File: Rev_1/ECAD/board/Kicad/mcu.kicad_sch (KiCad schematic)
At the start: 11 parts, among them Y100 16MHZ

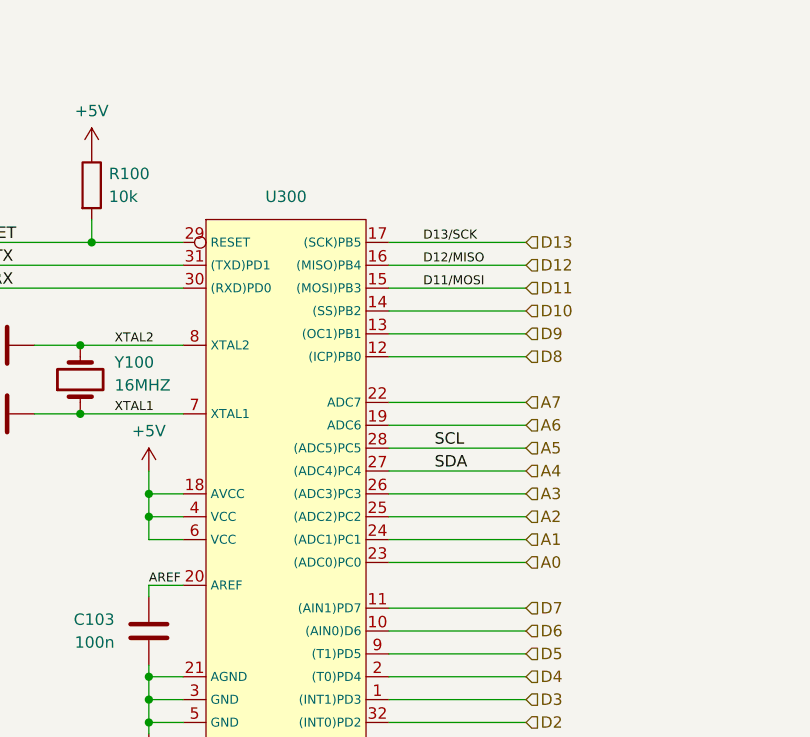
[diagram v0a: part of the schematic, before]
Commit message: Updated Symbol library´and added SD Card Reader to schematic
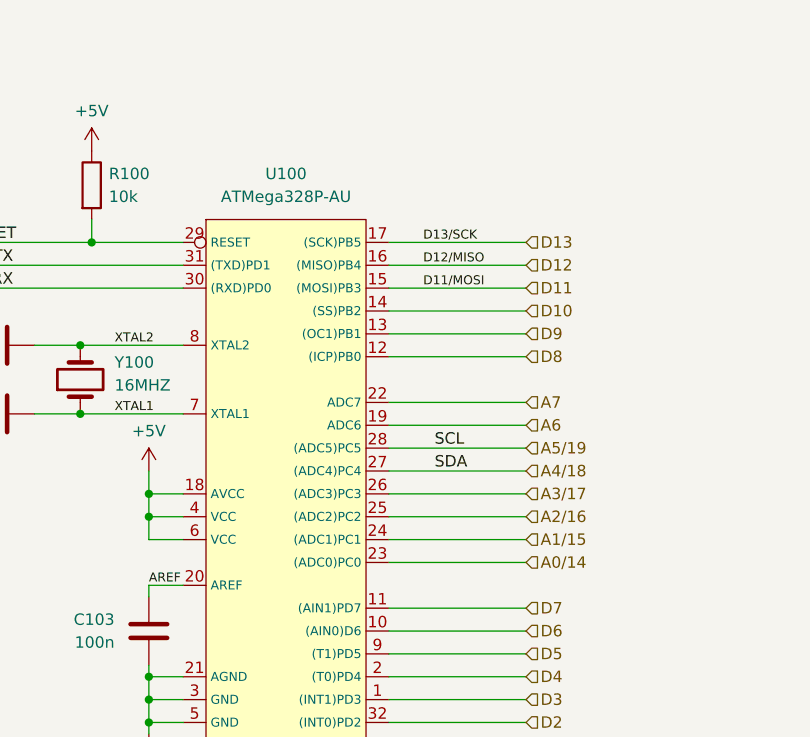
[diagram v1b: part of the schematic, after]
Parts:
- removed U300: ~, symbol EEPROM_PROGRAMER:ATMega328P-AU
- added U100: ATMega328P-AU, symbol EEPROM_PROGRAMMER:ATMega328P-AU
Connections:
- net +5V: now also U100.18 (AVCC), U100.4 (VCC), U100.6 (VCC)
- net A6: now also U100.19 (ADC6)
- net A7: now also U100.22 (ADC7)
- net AREF: now also U100.20 (AREF)
- net D10: now also U100.14 ((SS)PB2)
- net D11: now also U100.15 ((MOSI)PB3)
- net D12: now also U100.16 ((MISO)PB4)
- net D13: now also U100.17 ((SCK)PB5)
- net D2: now also U100.32 ((INT0)PD2)
- net D3: now also U100.1 ((INT1)PD3)
- net D4: now also U100.2 ((T0)PD4)
- net D5: now also U100.9 ((T1)PD5)
- net D6: now also U100.10 ((AIN0)D6)
- net D7: now also U100.11 ((AIN1)PD7)
- net D8: now also U100.12 ((ICP)PB0)
- net D9: now also U100.13 ((OC1)PB1)
- net GND: now also U100.21 (AGND), U100.3 (GND), U100.5 (GND)
- net RESET: now also U100.29 (RESET)
- net RX: now also U100.31 ((TXD)PD1)
- net TX: now also U100.30 ((RXD)PD0)
- net XTAL1: now also U100.7 (XTAL1)
- net XTAL2: now also U100.8 (XTAL2)
- new net A0/14: U100.23 ((ADC0)PC0)
- new net A1/15: U100.24 ((ADC1)PC1)
- new net A2/16: U100.25 ((ADC2)PC2)
- new net A3/17: U100.26 ((ADC3)PC3)
- new net A4/18: U100.27 ((ADC4)PC4)
- new net A5/19: U100.28 ((ADC5)PC5)

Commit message: Changes current limiting resistors for LEDS to 5k1 ohms
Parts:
- U100: footprint (none) -> EEPROM_PROGRAMMER:ATMega328P-AU
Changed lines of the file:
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@@
       (effects (font (size 1.27 1.27)))
     )
-    (property "Footprint" "" (at 143.51 87.63 0)
+    (property "Footprint" "EEPROM_PROGRAMMER:ATMega328P-AU" (at 143.51 87.63 0)
       (effects (font (size 1.27 1.27)) hide)
     )

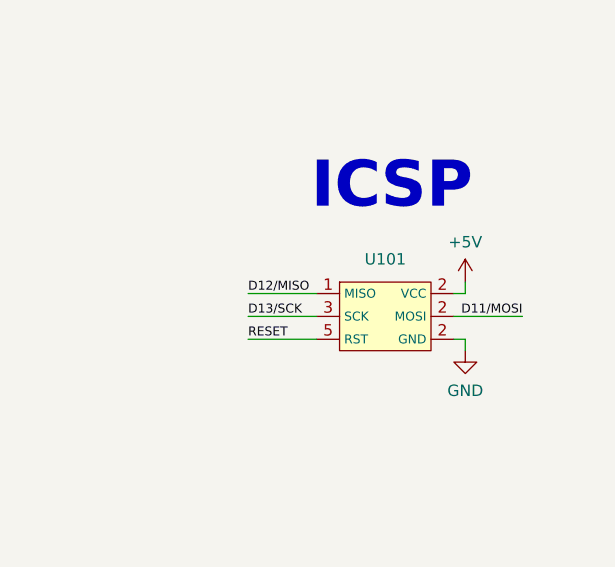
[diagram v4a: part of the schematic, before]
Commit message: Changed from 4-bit registers to shift registers
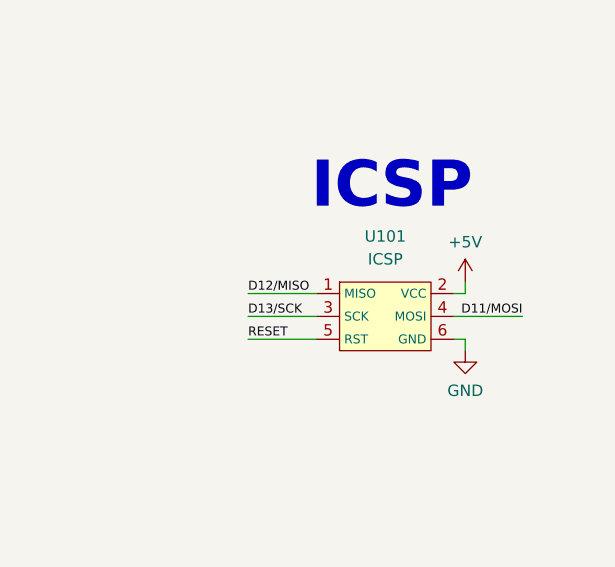
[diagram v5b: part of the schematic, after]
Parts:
- removed U101: ~, symbol EEPROM_PROGRAMER:ICSP
- added U101: ICSP, EEPROM_PROGRAMMER:ICSP, symbol EEPROM_PROGRAMMER:ICSP
- Y100: footprint (none) -> EEPROM_PROGRAMMER:Crystal
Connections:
- net +5V: now also U101.2 (VCC)
- net D11: now also U101.4 (MOSI)
- net D12: now also U101.1 (MISO)
- net D13: now also U101.3 (SCK)
- net GND: now also U101.6 (GND)
- net RESET: now also U101.5 (RST)
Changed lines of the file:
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@@
+    )
+  )
+  (symbol (lib_id "EEPROM_PROGRAMMER:ICSP") (at 234.95 102.87 0) (unit 1)
+    (in_bom yes) (on_board yes) (dnp no) (fields_autoplaced)
+    (property "Reference" "U101" (at 234.95 93.98 0)
+      (effects (font (size 1.27 1.27)))
+    )
+    (property "Value" "ICSP" (at 234.95 96.52 0)
+      (effects (font (size 1.27 1.27)))
+    )
+    (property "Footprint" "EEPROM_PROGRAMMER:ICSP" (at 234.95 92.71 0)
+      (effects (font (size 1.27 1.27)) hide)
+    )
+    (property "Datasheet" "" (at 234.95 102.87 0)
+      (effects (font (size 1.27 1.27)) hide)
+    )
+    (pin "1")
+    (pin "2")
+    (pin "3")
+    (pin "4")
+    (pin "5")
+    (pin "6")
+    (instances
+      (project "board"
+        (path "/2f4d49fd-9c63-4eb5-a266-4b5553b3e489/a9c4ef02-6c48-4ddc-bd95-3bc4e5cf2494"
+          (reference "U101") (unit 1)
+        )
+      )
     )
   )
@@
       (effects (font (size 1.27 1.27)) (justify right))
     )
-    (property "Footprint" "" (at 120.65 90.17 0)
-      (effects (font (size 1.27 1.27)) hide)
-    )
-    (property "Datasheet" "~" (at 120.65 90.17 0)
+    (property "Footprint" "EEPROM_PROGRAMMER:Crystal" (at 120.65 90.17 0)
+      (effects (font (size 1.27 1.27)) hide)
+    )
+    (property "Datasheet" "https://www.electrokit.com/kristall-16.0000-mhz-hc49/s" (at 120.65 90.17 0)
       (effects (font (size 1.27 1.27)) hide)
     )
@@
         )
       )
-    )
-  )
-  (symbol (lib_id "EEPROM_PROGRAMER:ICSP") (at 234.95 102.87 0) (unit 1)
-    (in_bom yes) (on_board yes) (dnp no) (fields_autoplaced)
-    (property "Reference" "U101" (at 234.95 96.52 0)
-      (effects (font (size 1.27 1.27)))
-    )
-    (property "Value" "~" (at 234.95 102.87 0)
-      (effects (font (size 1.27 1.27)))
-    )
-    (property "Footprint" "" (at 234.95 102.87 0)
-      (effects (font (size 1.27 1.27)) hide)
-    )
-    (property "Datasheet" "" (at 234.95 102.87 0)
-      (effects (font (size 1.27 1.27)) hide)
-    )
-    (pin "1")
-    (pin "2")
-    (pin "2")
-    (pin "2")
-    (pin "3")
-    (pin "5")
-    (instances
-      (project "board"
-        (path "/2f4d49fd-9c63-4eb5-a266-4b5553b3e489/a9c4ef02-6c48-4ddc-bd95-3bc4e5cf2494"
-          (reference "U101") (unit 1)
-        )
-      )
